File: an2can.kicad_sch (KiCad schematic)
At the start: 1 part

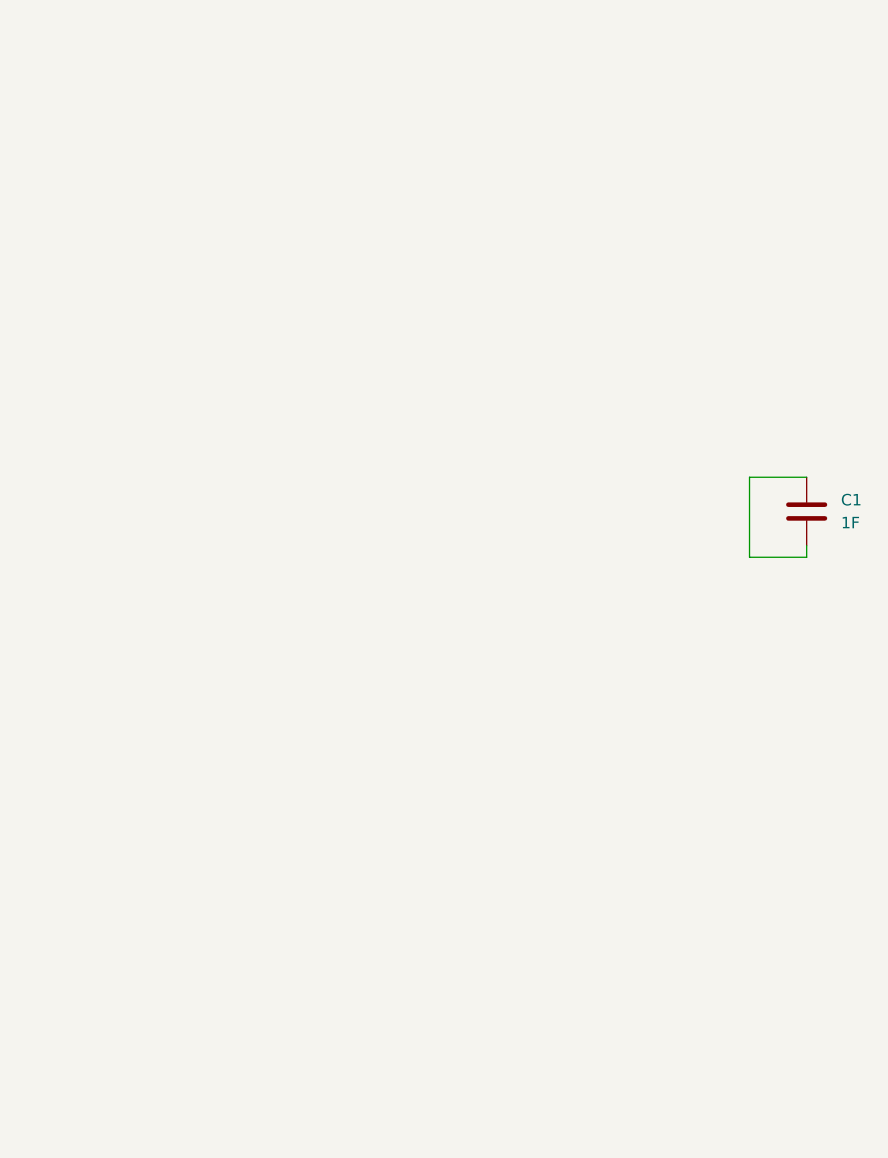
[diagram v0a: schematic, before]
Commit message: sch: first draft of mcu configuration
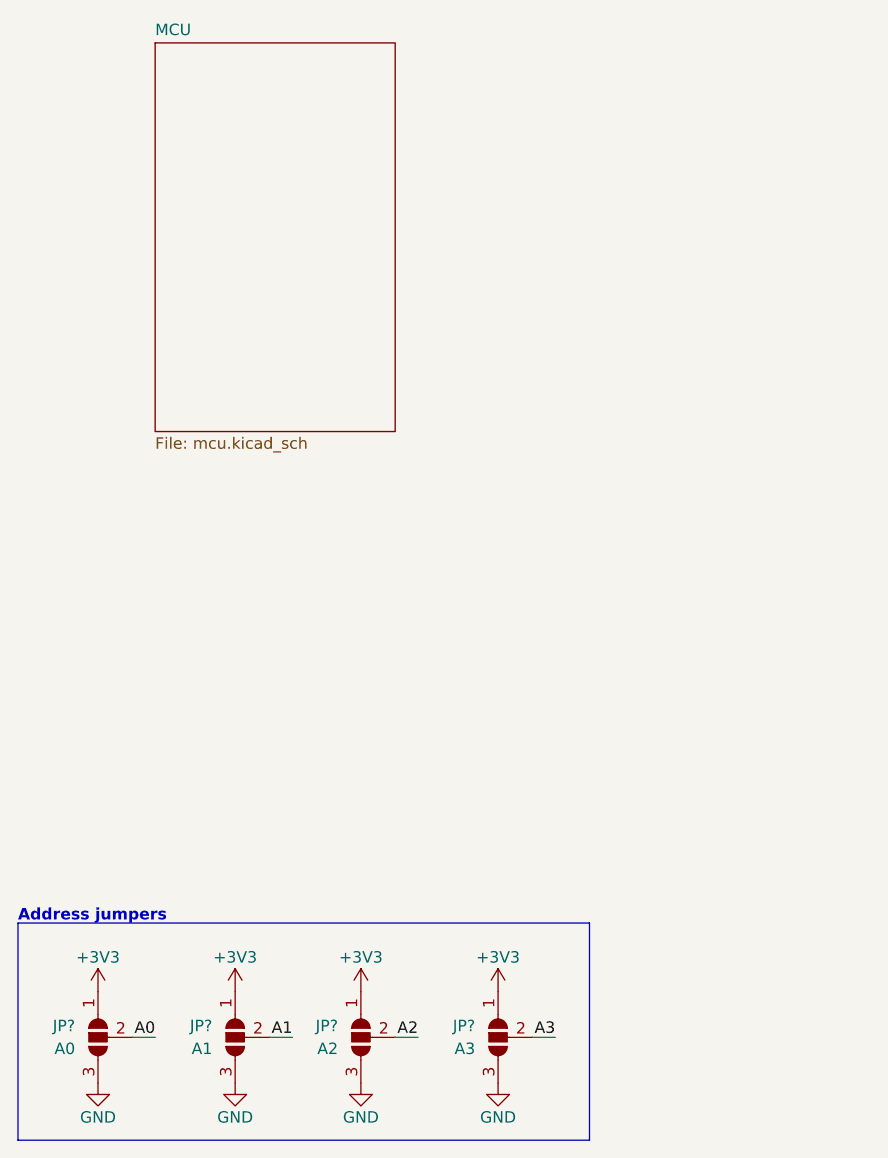
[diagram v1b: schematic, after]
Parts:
- removed C1: 1F, Capacitor_SMD:C_0805_2012Metric, symbol Device:C
- added JP?: A2, symbol Jumper:SolderJumper_3_Open
- added JP?: A3, symbol Jumper:SolderJumper_3_Open
- added JP?: A0, symbol Jumper:SolderJumper_3_Open
- added JP?: A1, symbol Jumper:SolderJumper_3_Open
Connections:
- new net +3V3: JP?.1 (A), JP?.1 (A), JP?.1 (A), JP?.1 (A)
- new net A0: JP?.2 (C)
- new net A1: JP?.2 (C)
- new net A2: JP?.2 (C)
- new net A3: JP?.2 (C)
- new net GND: JP?.3 (B), JP?.3 (B), JP?.3 (B), JP?.3 (B)
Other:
- added sheet MCU (mcu.kicad_sch)
- note added: "Address jumpers"
- title: Template -> An2CAN

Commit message: sch: add opamps
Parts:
- added C? (x14): 100n, Capacitor_SMD:C_0603_1608Metric, symbol Device:C
- added D? (x2): D_Schottky, Diode_SMD:D_SOD-523, symbol Device:D_Schottky
- added J?: Instr, symbol Connector_Generic:Conn_02x04_Counter_Clockwise
- added J?: GEN, symbol Connector_Generic:Conn_02x04_Counter_Clockwise
- added R? (x12): 1k8, Resistor_SMD:R_0603_1608Metric, symbol Device:R
- added R? (x2): R, Resistor_SMD:R_0603_1608Metric, symbol Device:R
- added R? (x8): 120 0.1%, Resistor_SMD:R_0603_1608Metric, symbol Device:R
- added R? (x2): 220k 0.1%, Resistor_SMD:R_0603_1608Metric, symbol Device:R_Small
- added RN? (x6): 100k, Resistor_SMD:R_Array_Convex_4x0603, symbol Device:R_Pack04_Split
- added RN? (x6): 18k, Resistor_SMD:R_Array_Convex_4x0603, symbol Device:R_Pack04_Split
- added RN? (x4): R, symbol Device:R_Pack04_Split
- added RN? (x6): 10k, Resistor_SMD:R_Array_Convex_4x0603, symbol Device:R_Pack04_Split
- added TP?: Offset, TestPoint:TestPoint_Pad_D1.0mm, symbol Connector:TestPoint
- added U? (x9): Opamp_Dual, symbol Device:Opamp_Dual
- added U? (x2): AD8221ARZ, Package_SO:MSOP-8_3x3mm_P0.65mm, symbol Eagle_Main:AD8221ARZ
- added U?: MAX6025, Package_TO_SOT_SMD:SOT-23, symbol Reference_Voltage:MAX6100
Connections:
- net A0: now also RN?.1 (R1.1); no longer JP?.2 (C)
- net A1: now also RN?.2 (R2.1); no longer JP?.2 (C)
- net A2: now also RN?.3 (R3.1); no longer JP?.2 (C)
- net A3: now also RN?.4 (R4.1); no longer JP?.2 (C)
- new net: R?.1, R?.2, U?.1 (x3)
- new net: R?.2, U?.2 (-) (x3)
- new net: C?.1, R?.1, RN?.3 (R3.1) (x3)
- new net: R?.1, U?.2 (Rg) (x2)
- new net: R?.2, U?.3 (Rg) (x2)
- new net: R?.1, U?.7 (x2)
- new net: C?.1, R?.1, RN?.4 (R4.1) (x3)
- new net: R?.1, R?.2, U?.7 (x3)
- new net: R?.2, U?.6 (-) (x3)
- new net: JP?.2 (C), RN?.7 (R2.2)
- new net: JP?.2 (C), RN?.6 (R3.2)
- new net: JP?.2 (C), RN?.5 (R4.2)
- new net: JP?.2 (C), RN?.8 (R1.2)
- new net +3.3VA: D?.1 (K), D?.1 (K)
- new net +5VA: C?.2, C?.2, C?.2, C?.2, C?.2, R?.1, R?.1, R?.1, R?.1, U?.1 (IN), U?.8 (V+), U?.8 (V+), U?.8 (V+), U?.8 (Vs+), U?.8 (Vs+)
- new net 2V5_OFFSET: C?.2, TP?.1, U?.2 (OUT), U?.6 (Ref), U?.6 (Ref)
- new net BPPS_1: RN?.4 (R4.1), RN?.4 (R4.1), RN?.4 (R4.1), RN?.5 (R4.2), RN?.5 (R4.2), RN?.5 (R4.2)
- new net BPPS_2: RN?.3 (R3.1), RN?.3 (R3.1), RN?.3 (R3.1), RN?.6 (R3.2), RN?.6 (R3.2), RN?.6 (R3.2)
- new net BPPS_S1: RN?.7 (R2.2), RN?.7 (R2.2), RN?.7 (R2.2), U?.3 (+), U?.3 (+), U?.3 (+)
- new net BPPS_S2: RN?.8 (R1.2), RN?.8 (R1.2), RN?.8 (R1.2), U?.5 (+), U?.5 (+), U?.5 (+)
- new net GNDA: C?.1, C?.1, C?.1, C?.1, C?.1, C?.1, C?.1, C?.1, C?.2, C?.2, C?.2, C?.2, C?.2, C?.2, R?.2, R?.2, R?.2, R?.2, RN?.1 (R1.1), RN?.1 (R1.1), RN?.1 (R1.1), RN?.2 (R2.1), RN?.2 (R2.1), RN?.2 (R2.1), RN?.5 (R4.2), RN?.5 (R4.2), RN?.5 (R4.2), RN?.6 (R3.2), RN?.6 (R3.2), RN?.6 (R3.2), U?.3 (GND), U?.4 (V-), U?.4 (V-), U?.4 (V-), U?.5 (Vs-), U?.5 (Vs-)
- new net SG_L1: C?.2, D?.2 (A), R?.2
- new net SG_L1-: R?.1, R?.2, U?.4 (+)
- new net SG_L2: C?.2, D?.2 (A), R?.2
- new net SG_L2+: R?.1, R?.2, U?.1 (-)
- new net SG_L3-: R?.1, R?.2, U?.4 (+)
- new net SG_L4+: R?.1, R?.2, U?.1 (-)
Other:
- note added: "Left 1"
- note added: "Left 2"
- note added: "Strain gauges"
- moved on the sheet: JP?

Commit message: sch: change to stm32l432k and change analog input topology
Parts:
- removed C? (x14): 100n, Capacitor_SMD:C_0603_1608Metric, symbol Device:C
- removed D? (x2): D_Schottky, Diode_SMD:D_SOD-523, symbol Device:D_Schottky
- removed R? (x12): 1k8, Resistor_SMD:R_0603_1608Metric, symbol Device:R
- removed R? (x2): R, Resistor_SMD:R_0603_1608Metric, symbol Device:R
- removed R? (x8): 120 0.1%, Resistor_SMD:R_0603_1608Metric, symbol Device:R
- removed R? (x2): 220k 0.1%, Resistor_SMD:R_0603_1608Metric, symbol Device:R_Small
- removed RN? (x6): 100k, Resistor_SMD:R_Array_Convex_4x0603, symbol Device:R_Pack04_Split
- removed RN? (x6): 18k, Resistor_SMD:R_Array_Convex_4x0603, symbol Device:R_Pack04_Split
- removed RN? (x6): 10k, Resistor_SMD:R_Array_Convex_4x0603, symbol Device:R_Pack04_Split
- removed TP?: Offset, TestPoint:TestPoint_Pad_D1.0mm, symbol Connector:TestPoint
- removed U? (x9): Opamp_Dual, symbol Device:Opamp_Dual
- removed U? (x2): AD8221ARZ, Package_SO:MSOP-8_3x3mm_P0.65mm, symbol Eagle_Main:AD8221ARZ
- removed U?: MAX6025, Package_TO_SOT_SMD:SOT-23, symbol Reference_Voltage:MAX6100
- added C?: 100n, Capacitor_SMD:C_0603_1608Metric, symbol Device:C
- added R?: R, symbol Device:R
- added TH?: Thermistor, symbol Device:Thermistor
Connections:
- net +3.3VA: now also TH?.1
- net GNDA: now also C?.1, R?.2
- new net Temp: C?.2, R?.1, TH?.2
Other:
- added sheet INA (ina.kicad_sch)
- added sheet OpAmp (opamp.kicad_sch)
- sheet MCU ports: added A0, A1, A2, A3, ADC_0, ADC_1, ADC_2, ADC_3, ADC_4, ADC_5, ADC_6, ADC_7, ADC_8; removed none
- note added: "Temperature"
- note removed: "Left 1"
- note removed: "Left 2"
- note removed: "Strain gauges"

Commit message: sch: input stage sheets
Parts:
- added C2: 100n, Capacitor_SMD:C_0603_1608Metric, symbol Device:C
- added TP1: Offset, TestPoint:TestPoint_Pad_D1.0mm, symbol Connector:TestPoint
- added U1: MAX6025, Package_TO_SOT_SMD:SOT-23, symbol Reference_Voltage:MAX6100
- JP1, JP2, JP3, JP4: renamed from JP?; footprint (none) -> Jumper:SolderJumper-3_P1.3mm_Open_RoundedPad1.0x1.5mm
- R1: renamed from R?; footprint (none) -> Resistor_SMD:R_0603_1608Metric
- RN1: renamed from RN?; footprint (none) -> Resistor_SMD:R_Array_Convex_4x0603
- TH1: renamed from TH?; footprint (none) -> Resistor_SMD:R_0603_1608Metric
- gave numbers to parts that had none: 3
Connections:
- net GNDA: now also C2.1, U1.3 (GND)
- new net +5VA: U1.1 (IN)
- new net 2V5_OFFSET: C2.2, TP1.1, U1.2 (OUT)
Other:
- sheet OpAmp renamed Input Stage 1
- removed sheet INA
- added sheet Input Stage 2 (input-stage.kicad_sch)
- added sheet Input Stage 3 (input-stage.kicad_sch)
- added sheet Input Stage 4 (input-stage.kicad_sch)
- sheet Input Stage 1: file opamp.kicad_sch -> input-stage.kicad_sch
- sheet Input Stage 1 ports: added OFFSET, OUT_COM, OUT_SINGLE, SG_H+, SG_H-, SG_L+, SG_L-; removed A0, A1, A2, A3, A4, A5, Analog_IN_0, Analog_IN_1, Analog_IN_2, Analog_IN_3, Analog_IN_4, Analog_IN_5

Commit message: sch: add power delivery network and finalize schematic
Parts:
- removed J1: Instr, symbol Connector_Generic:Conn_02x04_Counter_Clockwise
- removed J2: GEN, symbol Connector_Generic:Conn_02x04_Counter_Clockwise
- removed RN1: R, Resistor_SMD:R_Array_Convex_4x0603, symbol Device:R_Pack04_Split
- added C2, C3, C4: C, Capacitor_SMD:C_0805_2012Metric, symbol Device:C
- added C7: C, Capacitor_SMD:C_0603_1608Metric, symbol Device:C
- added FB1, FB2: FerriteBead, Inductor_SMD:L_0603_1608Metric, symbol Device:FerriteBead_Small
- added J1: PWR/CAN, Connector_Molex:Molex_Nano-Fit_105314-xx04_2x02_P2.50mm_Horizontal, symbol Connector_Generic:Conn_02x02_Top_Bottom
- added J5: Inputs, Connector_Molex:Molex_Nano-Fit_105314-xx16_2x08_P2.50mm_Horizontal, symbol Connector_Generic:Conn_02x08_Top_Bottom
- added U2: Tex_DCDC_v2, Eagle_Main:Tex_DCDC_v2_horizontal, symbol Eagle_Main:Tex_DCDC_v2
- renumbered C2 to C1, C1 to C6
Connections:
- net +3.3VA: now also U1.1 (IN), FB2.2
- net +3V3: now also C3.1, FB2.1, U2.1 (3V3)
- net +5VA: now also C4.1, C7.1, FB1.2, J5.11 (Pin_11), J5.13 (Pin_13), J5.15 (Pin_15), J5.9 (Pin_9); no longer U1.1 (IN)
- net A0: now also JP1.2 (C)
- net A1: now also JP2.2 (C)
- net A2: now also JP3.2 (C)
- net A3: now also JP4.2 (C)
- net GND: now also C2.2, C3.2, J1.4 (Pin_4), U2.2 (GND), U2.3 (GND), U2.6 (GND)
- net GNDA: now also C4.2, C7.2, J5.10 (Pin_10), J5.12 (Pin_12), J5.14 (Pin_14), J5.16 (Pin_16)
- new net +5V: C2.1, FB1.1, U2.4 (5V), U2.5 (5V)
- new net CAN+: J1.1 (Pin_1)
- new net CAN-: J1.2 (Pin_2)
- new net IN0: J5.1 (Pin_1)
- new net IN1: J5.2 (Pin_2)
- new net IN2: J5.3 (Pin_3)
- new net IN3: J5.4 (Pin_4)
- new net IN4: J5.5 (Pin_5)
- new net IN5: J5.6 (Pin_6)
- new net IN6: J5.7 (Pin_7)
- new net IN7: J5.8 (Pin_8)
- new net VDC: J1.3 (Pin_3), U2.7 (VIN)
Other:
- sheet Input Stage 1 ports: added SG_H-/IN0, SG_L+/IN1; removed SG_H-, SG_L+
- sheet Input Stage 2 ports: added SG_H-/IN0, SG_L+/IN1; removed SG_H-, SG_L+
- sheet Input Stage 3 ports: added SG_H-/IN0, SG_L+/IN1; removed SG_H-, SG_L+
- sheet Input Stage 4 ports: added SG_H-/IN0, SG_L+/IN1; removed SG_H-, SG_L+
- sheet MCU ports: added CAN+, CAN-; removed none
- note added: "Analog inputs"
- note added: "Caps are already present on DCDC Take voltage drop across bead into account"
- note added: "Caps are in MCU sheet"
- note added: "Connection point between GND and GNDA at MCU, as it has no VSSA"
- note added: "Could reduce pins by using less GNDA/+5VA if really needed"
- note added: "PDN"
- note added: "Populate only when using both positive and negative wheatstone bridge measurements"
- note added: "Power & CAN"
- note added: "Route +5VA and GNDA traces as if they were signals from the connector"
- note added: "Series resistors are in MCU sheet"
- note added: "Strain Gauge offset"
- note added: "Switching frequency is 500kHz considering R_{MODE1}=100k"
- moved on the sheet: C1, C6, JP2, JP3, JP4, R1, TH1, TP1, U1

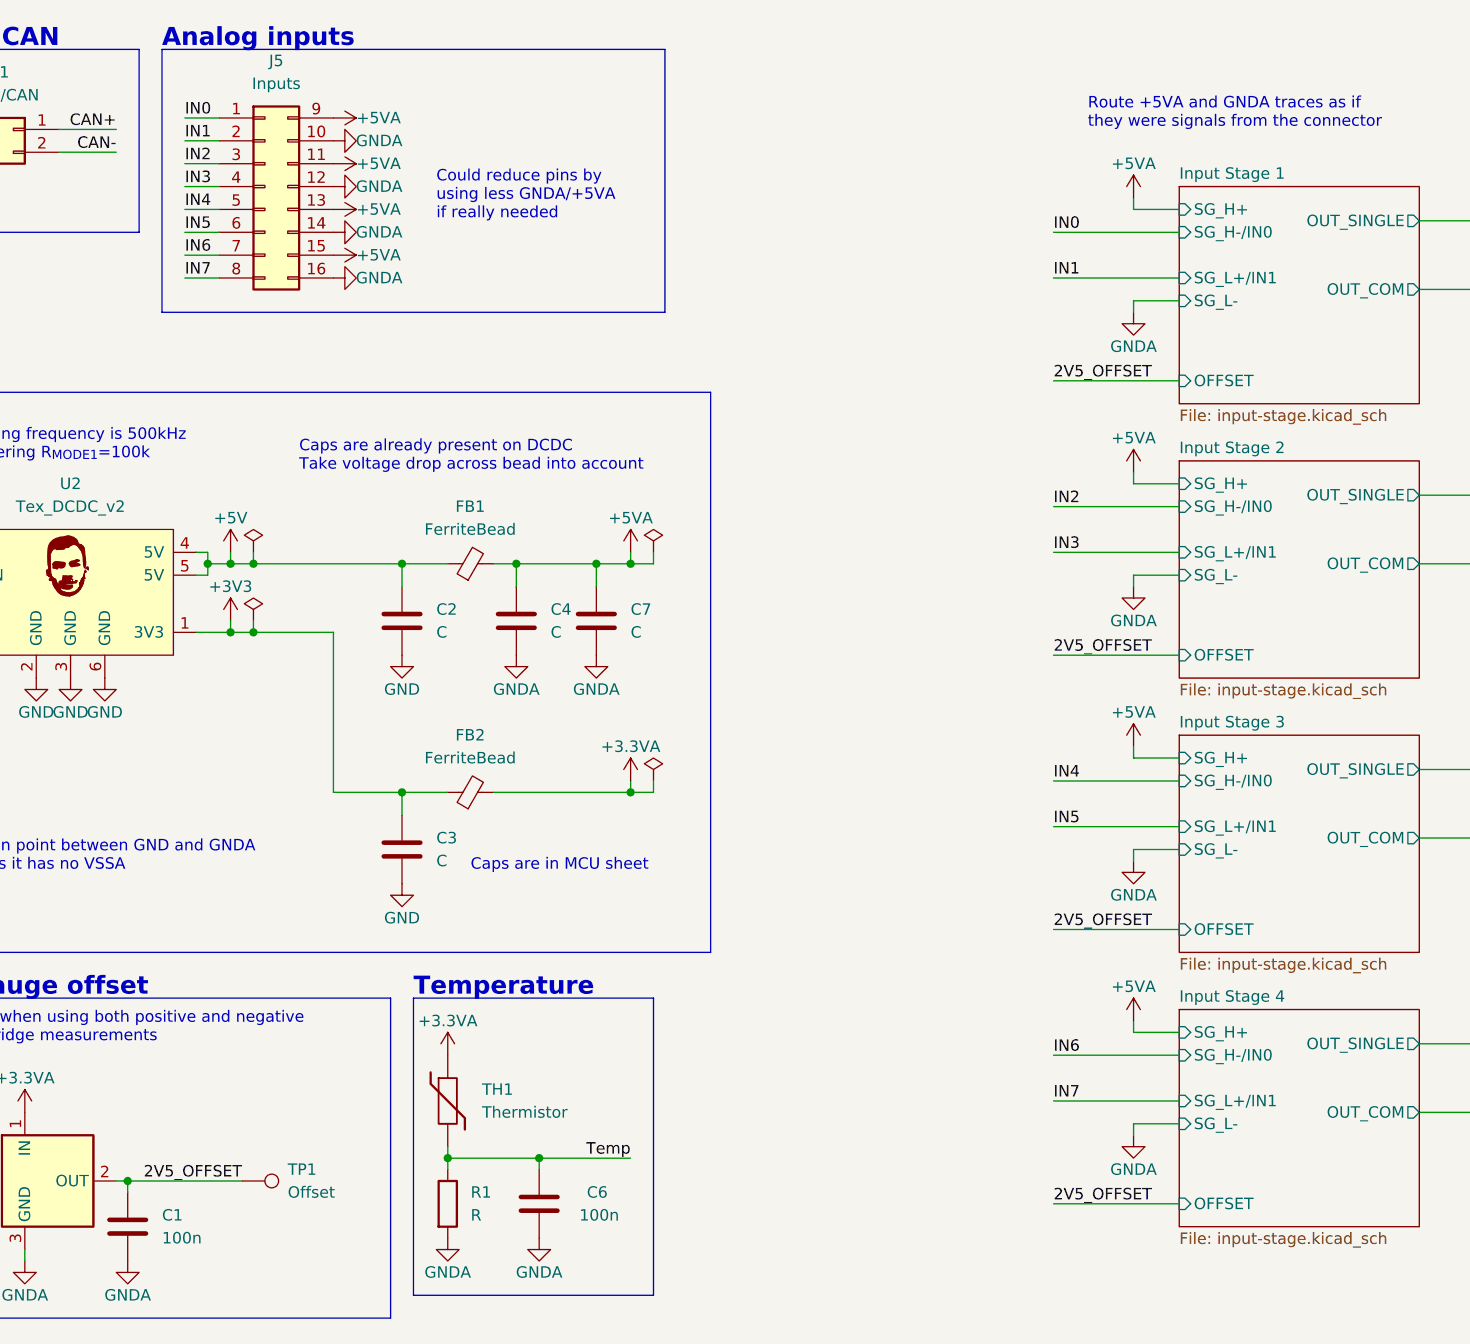
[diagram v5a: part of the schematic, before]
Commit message: sch: change single input connector to 4 02x02
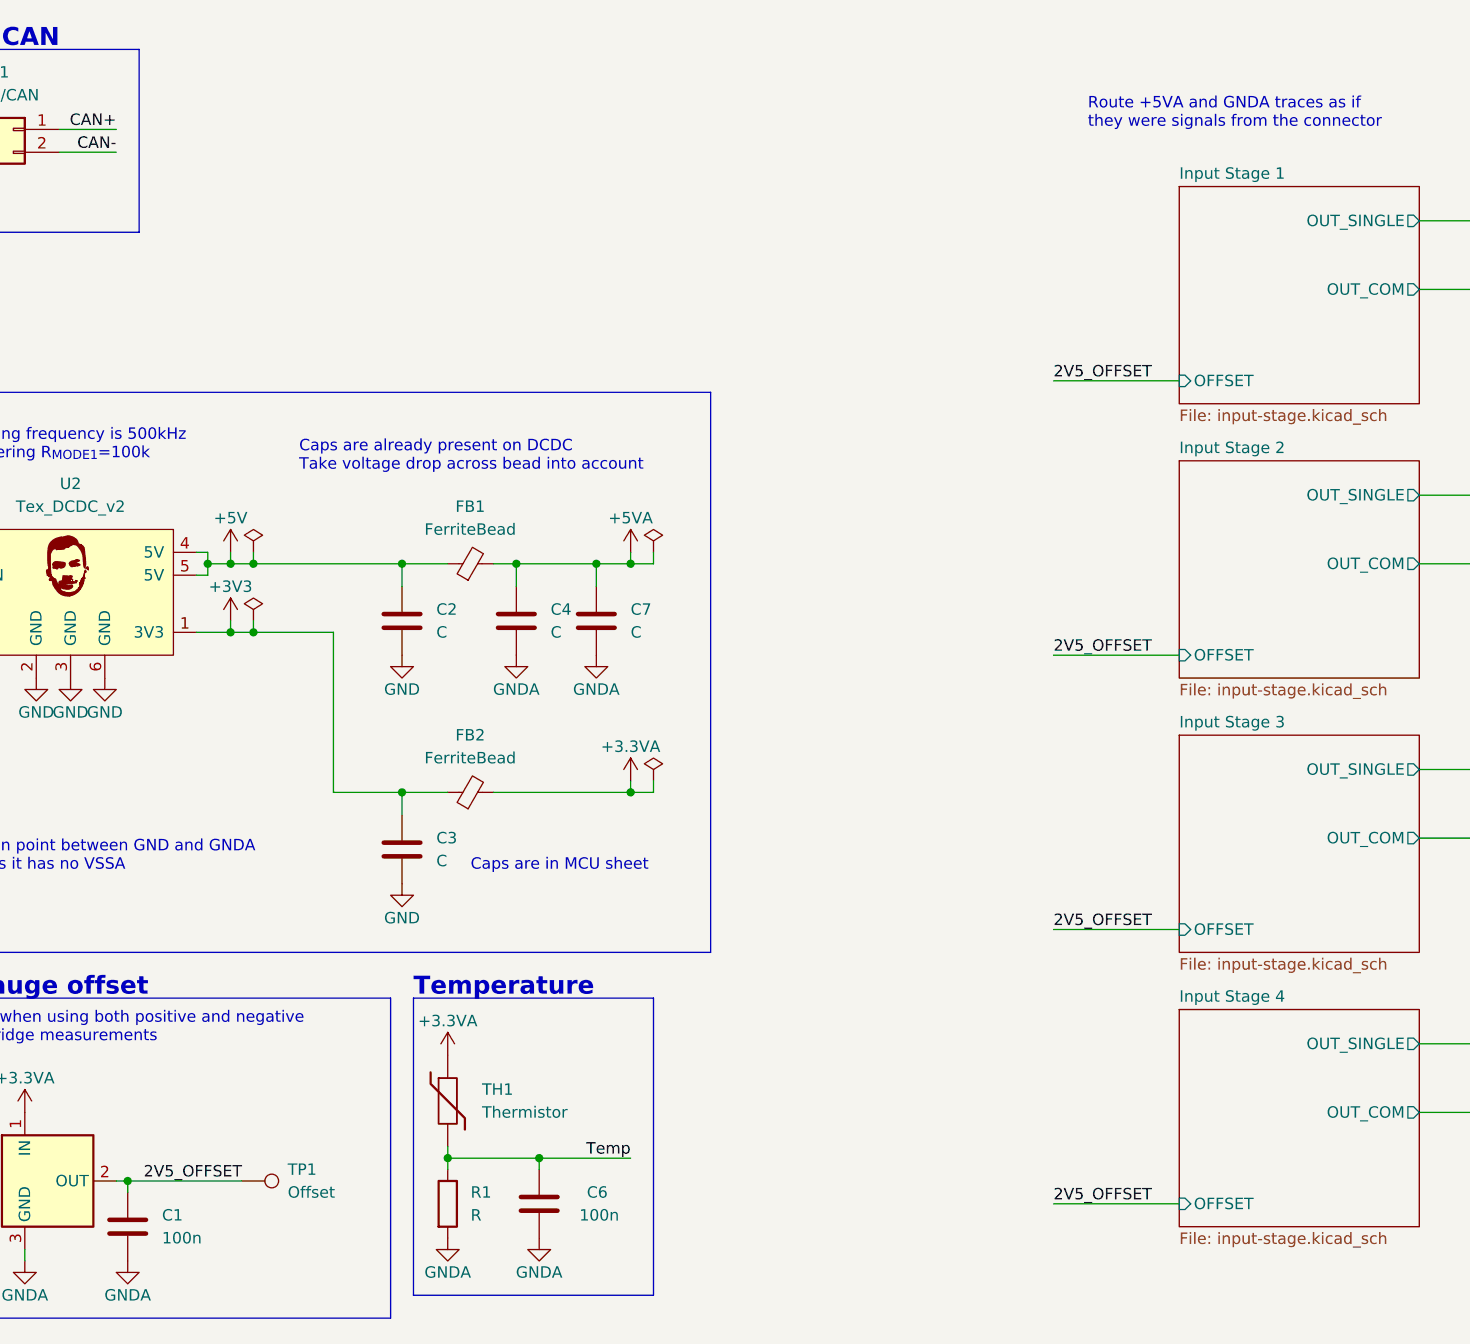
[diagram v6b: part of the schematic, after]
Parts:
- removed J5: Inputs, Connector_Molex:Molex_Nano-Fit_105314-xx16_2x08_P2.50mm_Horizontal, symbol Connector_Generic:Conn_02x08_Top_Bottom
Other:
- sheet Input Stage 1 ports: added none; removed SG_H+, SG_H-/IN0, SG_L+/IN1, SG_L-
- sheet Input Stage 2 ports: added none; removed SG_H+, SG_H-/IN0, SG_L+/IN1, SG_L-
- sheet Input Stage 3 ports: added none; removed SG_H+, SG_H-/IN0, SG_L+/IN1, SG_L-
- sheet Input Stage 4 ports: added none; removed SG_H+, SG_H-/IN0, SG_L+/IN1, SG_L-
- note removed: "Analog inputs"
- note removed: "Could reduce pins by using less GNDA/+5VA if really needed"
